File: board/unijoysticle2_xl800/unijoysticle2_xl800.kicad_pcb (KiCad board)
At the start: 4 copper layers, 72 x 52 mm, 53 parts, among them J1 USB_B_Micro, J2 DE9_Receptacle, J3 DE9_Receptacle, Q1 S8050, Q2 S8050, SW1 RESET, SW2 BOOT, SW3 MODE, SW4 SWAP, U1 ESP32-WROOM-32E, U2 AMS1117-3.3, U3 CH340C, U4 74HC05, U5 74HC05, U6 74HC05

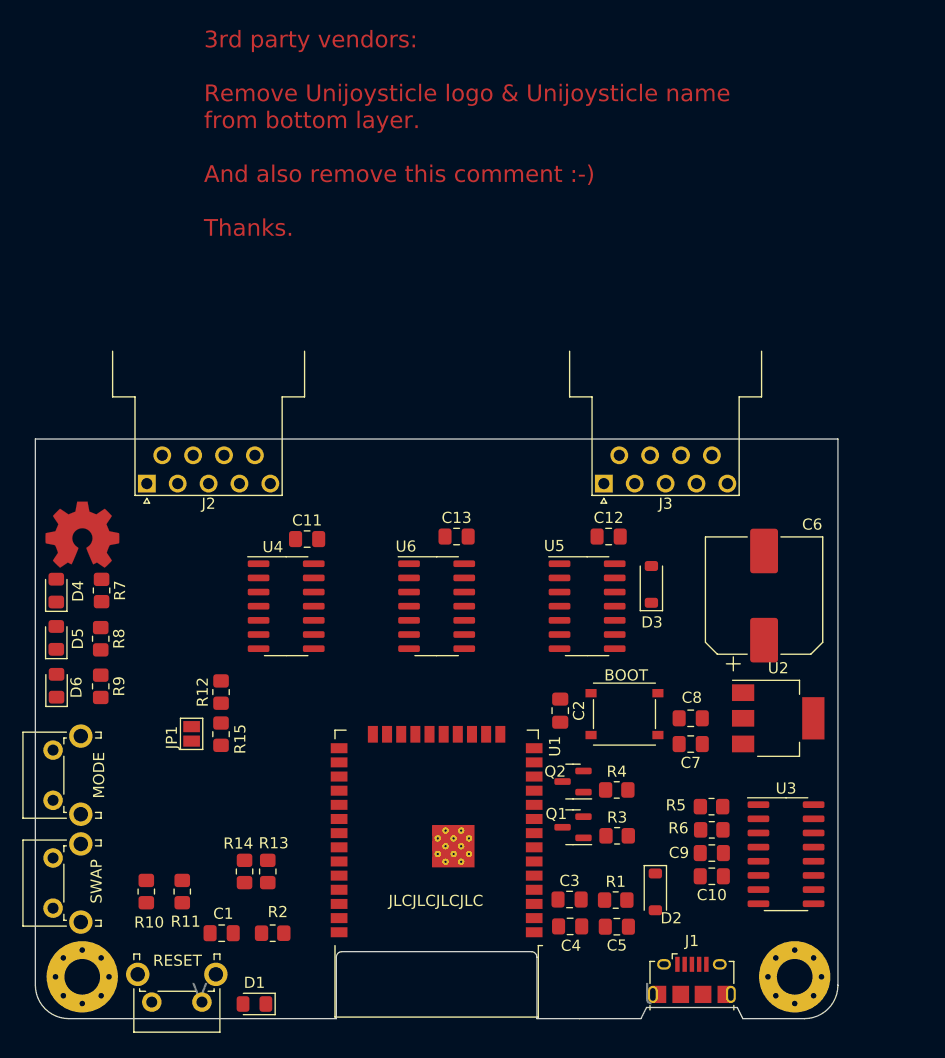
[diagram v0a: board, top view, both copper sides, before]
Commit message: 800xl: routes added
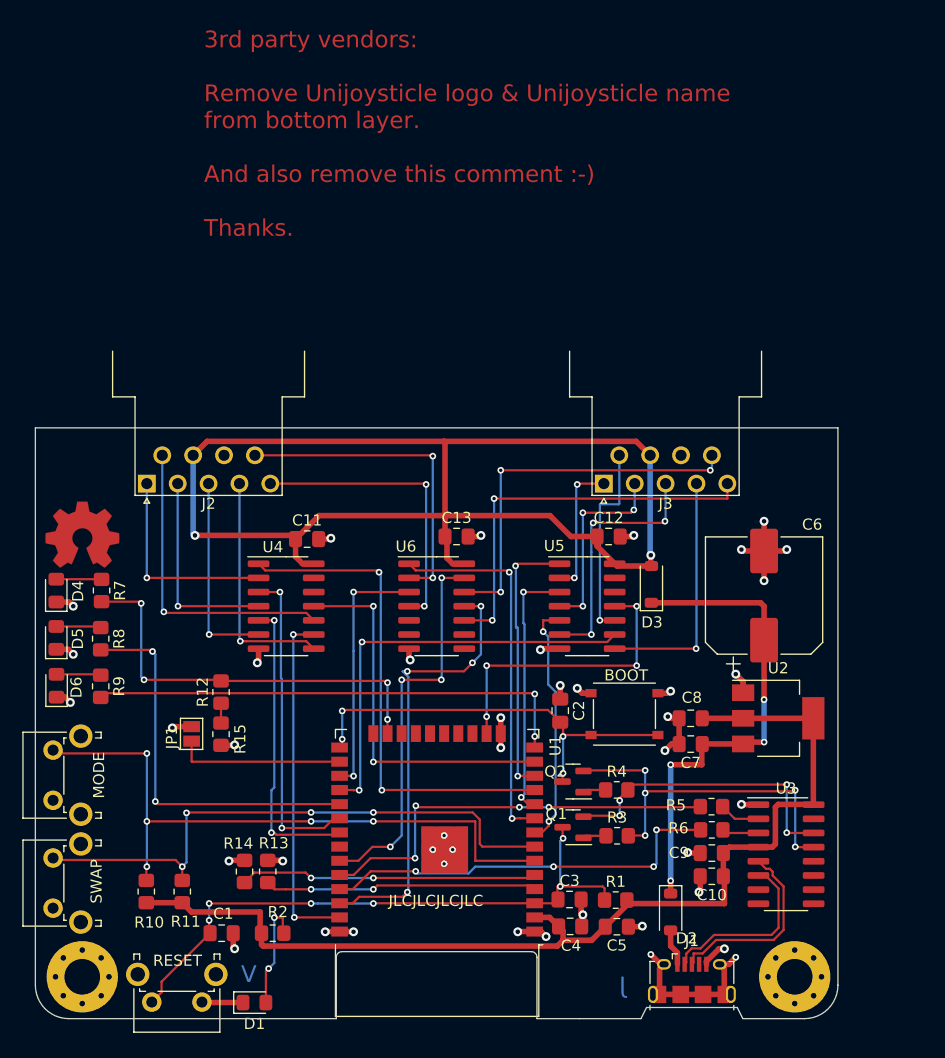
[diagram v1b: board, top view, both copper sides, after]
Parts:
- C6: value 1500uF -> 2200uF
- U1: value ESP32-WROOM-32E -> ESP32-WROOM-32; footprint RF_Module:ESP32-WROOM-32D -> Unijoysticle:ESP32-WROOM-32
- moved D2 2.27 mm to (134.5, 138.4)
- moved D1 0.13 mm to (97.2, 146.6), turned to 0 degrees
- moved U1 0.08 mm to (113.5, 131.9)
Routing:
- net +5V: track 0.00 -> 119.4 mm, vias 0 -> 2
- net +3V3: track 0.00 -> 95.2 mm
- net GND: track 0.00 -> 62.0 mm, vias 0 -> 40
- net GPIO_SWITCH_USER1: track 0.00 -> 58.3 mm, vias 0 -> 5
- net /ESP32/ESP_EN: track 0.00 -> 54.5 mm, vias 0 -> 6
- net GPIO_SWITCH_USER2: track 0.00 -> 51.9 mm, vias 0 -> 4
- net GPIO_J1_UP: track 0.00 -> 44.5 mm, vias 0 -> 2
- net Net-(D2-K): track 0.00 -> 44.3 mm, vias 0 -> 4
- net GPIO_LED_J2: track 0.00 -> 43.9 mm, vias 0 -> 2
- net GPIO_J2_POTY: track 0.00 -> 40.0 mm, vias 0 -> 4
- net GPIO_J2_RIGHT: track 0.00 -> 38.1 mm, vias 0 -> 2
- net UART_TX: track 0.00 -> 37.7 mm, vias 0 -> 4
- net /ESP32/ESP_BOOT: track 0.00 -> 37.4 mm, vias 0 -> 4
- net GPIO_BOOTSTRAP_15_LED_BT: track 0.00 -> 37.1 mm, vias 0 -> 4
- net UART_RX: track 0.00 -> 36.5 mm, vias 0 -> 4
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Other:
- board size 72 x 52 mm -> 72 x 53 mm

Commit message: Unijoysticle2 800X/A1000: fix warnings
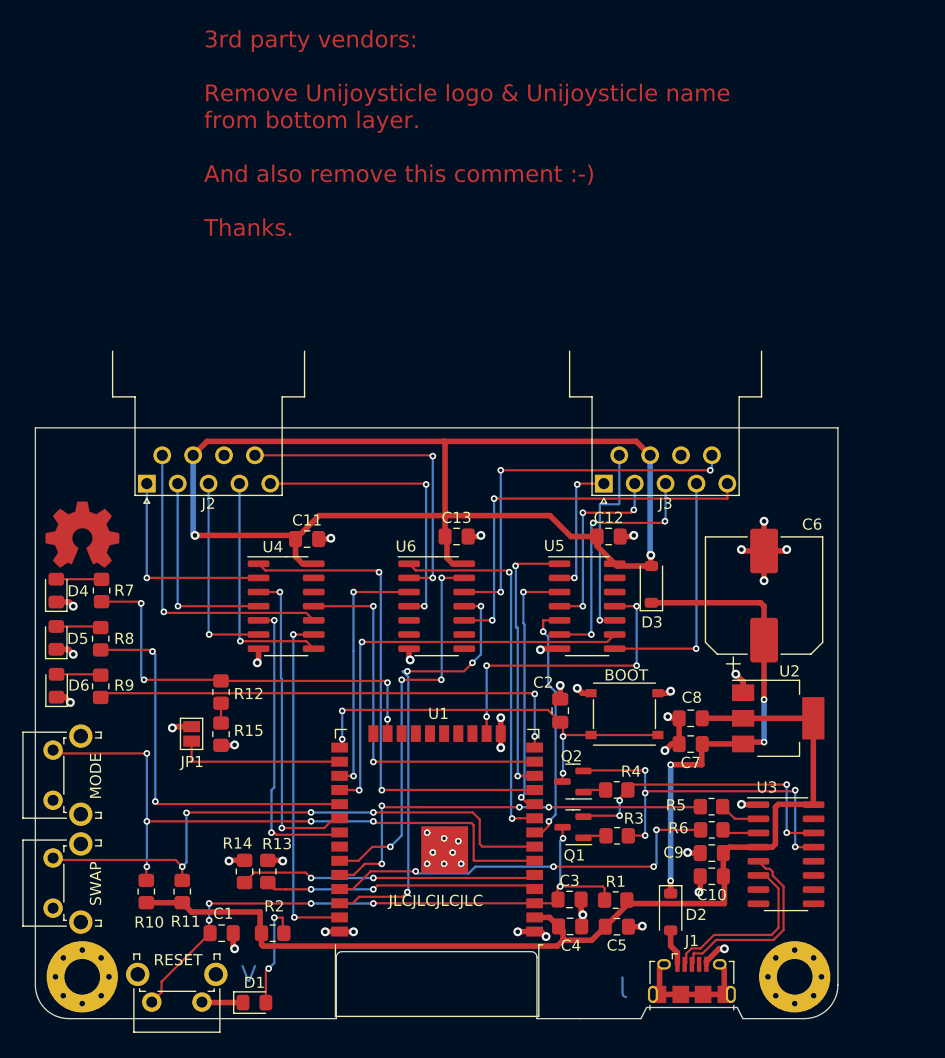
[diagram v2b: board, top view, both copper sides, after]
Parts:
- added G***: LOGO, Unijoysticle:unijoysticle_logo, B.Cu at (115.4, 113.8)
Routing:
- net unconnected-(J1-Shield-Pad6): track 14.8 -> 11.8 mm, vias 2 -> 0
- net GND: track 62.0 -> 63.4 mm, vias 40 -> 44
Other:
- board text added: "Unijoysticle 2 A1000 / 800XL Rev. A"
- board text removed: "Unijoysticle 2 XL800 Rev. A"
